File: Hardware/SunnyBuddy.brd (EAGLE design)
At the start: 47 x 47 mm, 33 parts, among them J1 5.5x2.1mm Barrel, J3 POWER_JACKPTH, J5 M02PTH, J6 M023.5MM, J7 M023.5MM, J8 M023.5MM, U1 LT3652

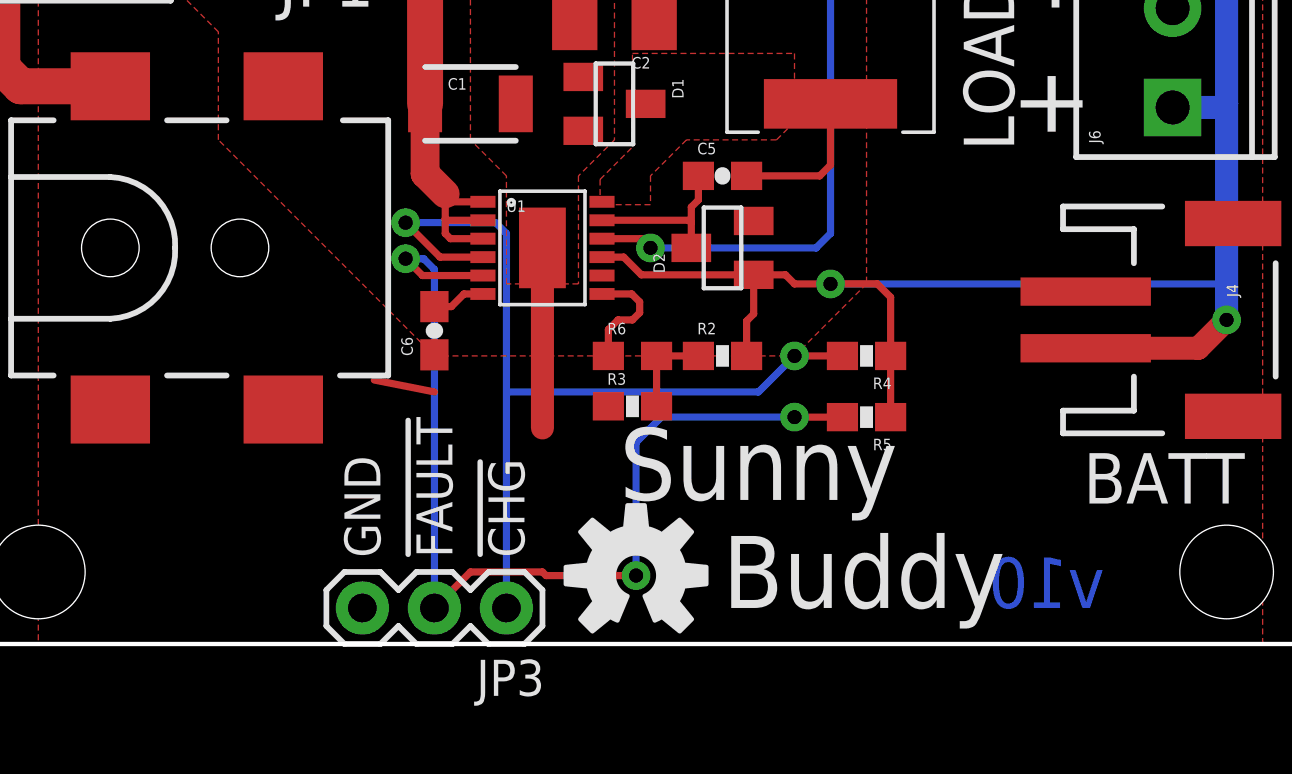
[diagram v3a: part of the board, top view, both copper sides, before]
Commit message: Add trimpot, adjust output res values
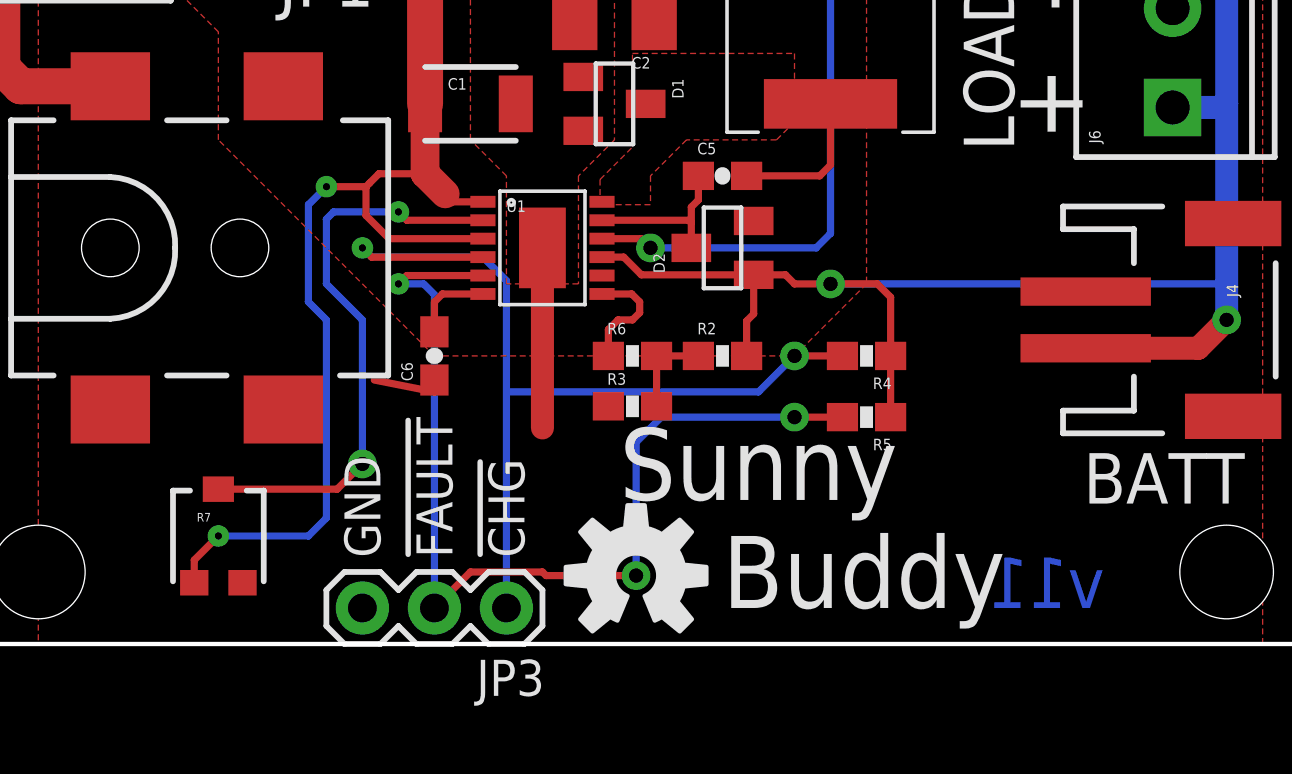
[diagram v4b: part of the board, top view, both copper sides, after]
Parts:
- added R7: 10k, SparkFun-Electromechanical:TRIMPOT-3MM
- R2: value 100k -> 47k
- R3: value 300k -> 220k
- R6: value 0 -> 220k; device SparkFun-Resistors:0603 -> SparkFun-Resistors:0603-RES
- moved C6 0.89 mm to (16.5, 10.2)
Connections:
- new net N$4: R7.2, U1.2
- net GND: now also R7.3
- net VIN: now also R7.1; no longer U1.2
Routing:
- net VIN: track 23.5 -> 46.8 mm, vias 0 -> 2
- net N$4: track 0.00 -> 20.4 mm, vias 0 -> 2
- net !CHRG: track 32.5 -> 33.9 mm
- net TIMER: track 1.89 -> 2.88 mm
- net !FAULT: track 36.1 -> 35.6 mm
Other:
- board text added: "v11"
- board text removed: "v10"
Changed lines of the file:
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@@
 <text x="18.288" y="30.48" size="1.778" layer="21" font="vector" ratio="15" rot="R90" align="bottom-center">JP2</text>
 <text x="82.55" y="-26.67" size="1.778" layer="51" font="vector" ratio="15" align="bottom-center">M. Hord</text>
-<text x="38.1" y="1.27" size="1.778" layer="16" font="vector" ratio="15" rot="MR0" align="bottom-center">v10</text>
+<text x="38.1" y="1.27" size="1.778" layer="16" font="vector" ratio="15" rot="MR0" align="bottom-center">v11</text>
 <text x="3.302" y="40.767" size="1.778" layer="21" font="vector" ratio="15">SOLAR IN</text>
 <text x="40.64" y="24.892" size="1.778" layer="21" font="vector" ratio="15" rot="R90">LOAD</text>
@@
 <attribute name="PROD_ID" value="CONN-08352" x="19.05" y="-21.59" size="1.778" layer="27" rot="R270" display="off"/>
 </element>
-<element name="C6" library="SparkFun-Capacitors" package="0603-CAP" value="1.0uF" x="16.51" y="11.049" rot="R90">
-<attribute name="PROD_ID" value="CAP-00868" x="76.2" y="38.989" size="1.778" layer="27" rot="R90" display="off"/>
-</element>
-<element name="R3" library="SparkFun-Resistors" package="0603-RES" value="300k" x="23.495" y="8.382">
-<attribute name="PROD_ID" value="RES-10809" x="59.055" y="-51.308" size="1.778" layer="27" display="off"/>
-</element>
-<element name="R2" library="SparkFun-Resistors" package="0603-RES" value="100k" x="26.67" y="10.16">
-<attribute name="PROD_ID" value="RES-07828" x="58.42" y="-49.53" size="1.778" layer="27" display="off"/>
+<element name="C6" library="SparkFun-Capacitors" package="0603-CAP" value="1.0uF" x="16.51" y="10.16" rot="R90">
+<attribute name="PROD_ID" value="CAP-00868" x="76.2" y="38.1" size="1.778" layer="27" rot="R90" display="off"/>
+</element>
+<element name="R3" library="SparkFun-Resistors" package="0603-RES" value="220k" x="23.495" y="8.382">
+<attribute name="PROD_ID" value="RES-08969" x="59.055" y="-51.308" size="1.778" layer="27" display="off"/>
+</element>
+<element name="R2" library="SparkFun-Resistors" package="0603-RES" value="47k" x="26.67" y="10.16">
+<attribute name="PROD_ID" value="RES-07871" x="58.42" y="-49.53" size="1.778" layer="27" display="off"/>
 </element>
 <element name="J5" library="SparkFun-Connectors" package="1X02" value="M02PTH" x="44.45" y="26.67" rot="R90"/>
@@
 </element>
 <element name="JP3" library="SparkFun-Connectors" package="1X03" value="" x="19.05" y="1.27" rot="R180"/>
-<element name="R6" library="SparkFun-Resistors" package="0603" value="0" x="23.495" y="10.16">
-<attribute name="PROD_ID" value="RES-08609" x="23.495" y="10.16" size="1.778" layer="27" font="vector" ratio="15" display="off"/>
+<element name="R6" library="SparkFun-Resistors" package="0603-RES" value="220k" x="23.495" y="10.16">
+<attribute name="PROD_ID" value="RES-08969" x="23.495" y="10.16" size="1.778" layer="27" font="vector" ratio="15" display="off"/>
+</element>
+<element name="R7" library="SparkFun-Electromechanical" package="TRIMPOT-3MM" value="10k" x="8.89" y="3.81">
+<attribute name="PROD_ID" value="RES-09285" x="8.89" y="3.81" size="1.778" layer="27" font="vector" ratio="15" display="off"/>
 </element>
 </elements>
@@
 <contactref element="C1" pad="1"/>
 <contactref element="U1" pad="3"/>
-<contactref element="U1" pad="2"/>
 <contactref element="JP1" pad="2"/>
 <contactref element="JP2" pad="2"/>
@@
 <wire x1="18.22" y1="15.595" x2="17.171" y2="15.595" width="0.254" layer="1"/>
 <wire x1="17.171" y1="15.595" x2="16.891" y2="15.875" width="0.254" layer="1"/>
-<wire x1="18.22" y1="14.295" x2="17.074" y2="14.295" width="0.254" layer="1"/>
-<wire x1="17.074" y1="14.295" x2="16.891" y2="14.478" width="0.254" layer="1"/>
-<wire x1="16.891" y1="14.478" x2="16.891" y2="14.986" width="0.254" layer="1"/>
-<wire x1="16.891" y1="14.986" x2="16.891" y2="15.875" width="0.254" layer="1"/>
-<wire x1="18.22" y1="14.945" x2="16.932" y2="14.945" width="0.254" layer="1"/>
-<wire x1="16.932" y1="14.945" x2="16.891" y2="14.986" width="0.254" layer="1"/>
+<contactref element="R7" pad="1"/>
+<wire x1="18.22" y1="14.295" x2="14.915" y2="14.295" width="0.254" layer="1"/>
+<wire x1="14.915" y1="14.295" x2="14.097" y2="15.113" width="0.254" layer="1"/>
+<wire x1="14.097" y1="15.113" x2="14.097" y2="16.129" width="0.254" layer="1"/>
+<wire x1="14.224" y1="16.256" x2="14.554" y2="16.586" width="0.254" layer="1"/>
+<wire x1="16.18" y1="16.586" x2="14.554" y2="16.586" width="0.254" layer="1"/>
+<wire x1="8.04" y1="2.16" x2="8.04" y2="2.96" width="0.254" layer="1"/>
+<wire x1="8.04" y1="2.96" x2="8.89" y2="3.81" width="0.254" layer="1"/>
+<via x="8.89" y="3.81" extent="1-16" drill="0.254"/>
+<wire x1="8.89" y1="3.81" x2="12.065" y2="3.81" width="0.254" layer="16"/>
+<wire x1="12.065" y1="3.81" x2="12.7" y2="4.445" width="0.254" layer="16"/>
+<wire x1="12.7" y1="4.445" x2="12.7" y2="11.43" width="0.254" layer="16"/>
+<wire x1="12.7" y1="11.43" x2="12.065" y2="12.065" width="0.254" layer="16"/>
+<wire x1="12.065" y1="12.065" x2="12.065" y2="15.494" width="0.254" layer="16"/>
+<wire x1="12.065" y1="15.494" x2="12.7" y2="16.129" width="0.254" layer="16"/>
+<via x="12.7" y="16.129" extent="1-16" drill="0.254"/>
+<wire x1="12.7" y1="16.129" x2="14.097" y2="16.129" width="0.254" layer="1"/>
+<wire x1="14.097" y1="16.129" x2="14.224" y2="16.256" width="0.254" layer="1"/>
 </signal>
 <signal name="GND">
@@
 <contactref element="J1" pad="GND"/>
 <contactref element="JP3" pad="3"/>
+<contactref element="R7" pad="3"/>
 </signal>
 <signal name="BOOST">
@@
 <contactref element="C6" pad="2"/>
 <contactref element="U1" pad="6"/>
-<wire x1="18.22" y1="12.345" x2="17.552" y2="12.345" width="0.254" layer="1"/>
-<wire x1="16.51" y1="11.899" x2="17.106" y2="11.899" width="0.254" layer="1"/>
-<wire x1="17.106" y1="11.899" x2="17.552" y2="12.345" width="0.254" layer="1"/>
+<wire x1="18.22" y1="12.345" x2="16.79" y2="12.345" width="0.254" layer="1"/>
+<wire x1="16.79" y1="12.345" x2="16.51" y2="12.065" width="0.254" layer="1"/>
+<wire x1="16.51" y1="12.065" x2="16.51" y2="11.01" width="0.254" layer="1"/>
 </signal>
 <signal name="FB">
@@
 <contactref element="R4" pad="2"/>
 <contactref element="JP3" pad="1"/>
-<wire x1="18.22" y1="13.645" x2="16.708" y2="13.645" width="0.254" layer="1"/>
-<wire x1="16.708" y1="13.645" x2="15.494" y2="14.859" width="0.254" layer="1"/>
-<via x="15.494" y="14.859" extent="1-16" drill="0.508"/>
-<wire x1="15.494" y1="14.859" x2="18.669" y2="14.859" width="0.254" layer="16"/>
-<wire x1="18.669" y1="14.859" x2="19.05" y2="14.478" width="0.254" layer="16"/>
-<wire x1="19.05" y1="14.478" x2="19.05" y2="8.89" width="0.254" layer="16"/>
+<wire x1="19.05" y1="12.815" x2="19.05" y2="8.89" width="0.254" layer="16"/>
 <wire x1="19.05" y1="8.89" x2="19.05" y2="1.27" width="0.254" layer="16"/>
 <wire x1="27.94" y1="8.89" x2="19.05" y2="8.89" width="0.254" layer="16"/>
@@
 <via x="29.21" y="10.16" extent="1-16" drill="0.508"/>
 <wire x1="27.94" y1="8.89" x2="29.21" y2="10.16" width="0.254" layer="16"/>
+<wire x1="18.22" y1="13.645" x2="14.295" y2="13.645" width="0.254" layer="1"/>
+<wire x1="14.295" y1="13.645" x2="13.97" y2="13.97" width="0.254" layer="1"/>
+<via x="13.97" y="13.97" extent="1-16" drill="0.254"/>
+<wire x1="19.05" y1="12.815" x2="18.22" y2="13.645" width="0.254" layer="16"/>
+<wire x1="18.22" y1="13.645" x2="14.295" y2="13.645" width="0.254" layer="16"/>
+<wire x1="14.295" y1="13.645" x2="13.97" y2="13.97" width="0.254" layer="16"/>
 </signal>
 <signal name="!FAULT">
@@
 <contactref element="R5" pad="2"/>
 <contactref element="JP3" pad="2"/>
-<wire x1="18.22" y1="12.995" x2="16.088" y2="12.995" width="0.254" layer="1"/>
-<wire x1="16.088" y1="12.995" x2="15.494" y2="13.589" width="0.254" layer="1"/>
-<via x="15.494" y="13.589" extent="1-16" drill="0.508"/>
-<wire x1="15.494" y1="13.589" x2="16.129" y2="13.589" width="0.254" layer="16"/>
-<wire x1="16.129" y1="13.589" x2="16.51" y2="13.208" width="0.254" layer="16"/>
-<wire x1="16.51" y1="13.208" x2="16.51" y2="1.27" width="0.254" layer="16"/>
+<wire x1="16.51" y1="12.319" x2="16.51" y2="1.27" width="0.254" layer="16"/>
 <wire x1="23.622" y1="7.112" x2="23.622" y2="2.413" width="0.254" layer="16"/>
 <via x="23.622" y="2.413" extent="1-16" drill="0.508"/>
@@
 <wire x1="23.622" y1="7.112" x2="24.511" y2="8.001" width="0.254" layer="16"/>
 <wire x1="24.511" y1="8.001" x2="29.21" y2="8.001" width="0.254" layer="16"/>
+<wire x1="18.22" y1="12.995" x2="15.535" y2="12.995" width="0.254" layer="1"/>
+<wire x1="15.535" y1="12.995" x2="15.24" y2="12.7" width="0.254" layer="1"/>
+<via x="15.24" y="12.7" extent="1-16" drill="0.254"/>
+<wire x1="15.24" y1="12.7" x2="16.129" y2="12.7" width="0.254" layer="16"/>
+<wire x1="16.129" y1="12.7" x2="16.51" y2="12.319" width="0.254" layer="16"/>
 </signal>
 <signal name="V_BATT">
@@
 <wire x1="22.645" y1="10.16" x2="22.645" y2="11.088" width="0.254" layer="1"/>
 </signal>
+<signal name="N$4">
+<contactref element="U1" pad="2"/>
+<contactref element="R7" pad="2"/>
+<wire x1="8.89" y1="5.46" x2="13.08" y2="5.46" width="0.254" layer="1"/>
+<wire x1="13.08" y1="5.46" x2="13.97" y2="6.35" width="0.254" layer="1"/>
+<via x="13.97" y="6.35" extent="1-16" drill="0.508"/>
+<wire x1="18.22" y1="14.945" x2="15.535" y2="14.945" width="0.254" layer="1"/>
+<wire x1="15.535" y1="14.945" x2="15.24" y2="15.24" width="0.254" layer="1"/>
+<via x="15.24" y="15.24" extent="1-16" drill="0.254"/>
+<wire x1="15.24" y1="15.24" x2="12.954" y2="15.24" width="0.254" layer="16"/>
+<wire x1="12.954" y1="15.24" x2="12.7" y2="14.986" width="0.254" layer="16"/>
+<wire x1="12.7" y1="14.986" x2="12.7" y2="12.7" width="0.254" layer="16"/>
+<wire x1="12.7" y1="12.7" x2="13.97" y2="11.43" width="0.254" layer="16"/>
+<wire x1="13.97" y1="11.43" x2="13.97" y2="6.35" width="0.254" layer="16"/>
+</signal>
 </signals>
